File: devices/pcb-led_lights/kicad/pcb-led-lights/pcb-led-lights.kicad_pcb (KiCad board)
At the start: 2 copper layers, 61 x 30 mm, 29 parts, among them J1 Screw_Terminal_01x12, Q1 SUD40N06-25L, Q2 SUD40N06-25L, Q3 SUD40N06-25L, Q4 SUD40N06-25L, Q5 SUD40N06-25L, Q6 SUD40N06-25L, Q7 SUD40N06-25L, U1 AP63203WU, U2 ESP32-WROOM-32

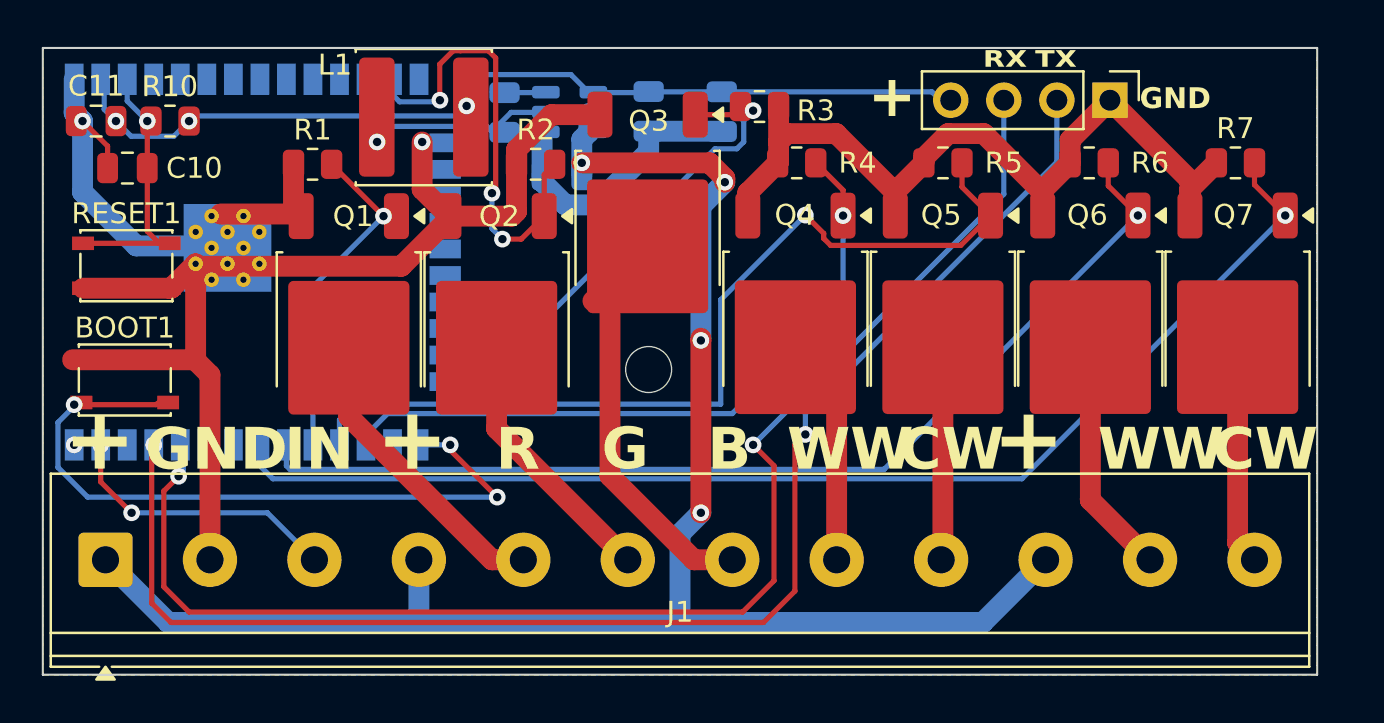
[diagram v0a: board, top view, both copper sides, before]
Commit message: use esp32-c6
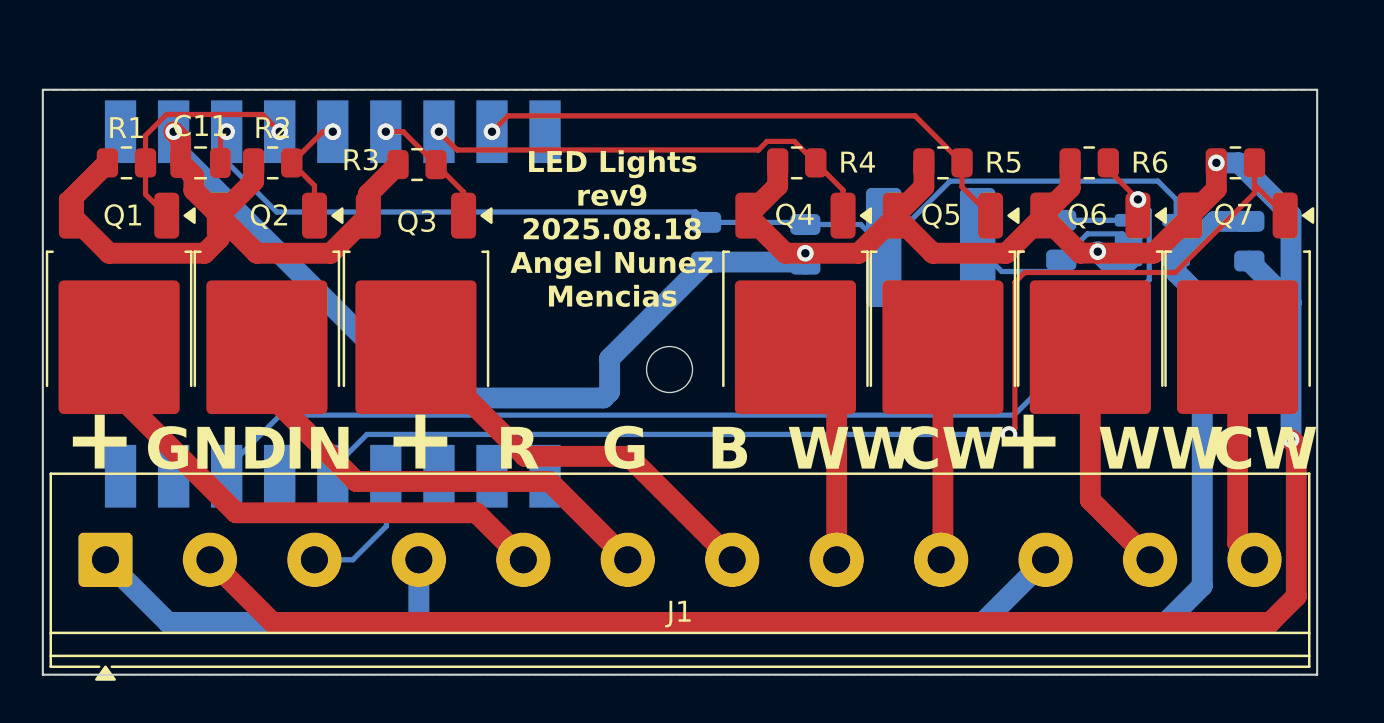
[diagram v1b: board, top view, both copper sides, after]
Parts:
- removed BOOT1, RESET1: SW_Push, Button_Switch_SMD:SW_SPST_PTS810
- removed C10: 10uF, Capacitor_SMD:C_0805_2012Metric
- removed R10: 12K, Resistor_SMD:R_0805_2012Metric
- removed U2: ESP32-WROOM-32, RF_Module:ESP32-WROOM-32
- removed program_port1: Conn_01x04_Male, Connector_PinHeader_2.54mm:PinHeader_1x04_P2.54mm_Vertical
- added U3: ESP32-C6 ZERO, Waveshare-ESP32:Waveshare-ESP32-C6-Zero, B.Cu at (47.6, 41.8)
- L1: moved to B.Cu
- moved C12 33.1 mm to (91.8, 39.2), turned to 90 degrees
- moved U1 28.6 mm to (87.1, 39.2)
- moved C1 27.3 mm to (82.8, 39.2)
- moved L1 25.1 mm to (76.5, 39.5), turned to 180 degrees
- moved R3 16.6 mm to (51.9, 35.6), turned to 0 degrees
- moved R2 12.6 mm to (45.0, 35.5)
- moved Q3 12.1 mm to (51.9, 43.1)
- moved Q1 11.0 mm to (37.7, 43.1)
- moved Q2 11.0 mm to (44.7, 43.1)
- moved C13 9.84 mm to (70.5, 39.4)
- moved R1 8.91 mm to (38.0, 35.5)
- moved C2 6.29 mm to (65.8, 39.3)
- moved C11 5.39 mm to (41.5, 35.5), turned to 180 degrees
- moved H1 1.00 mm to (64.0, 45.4), turned to 90 degrees
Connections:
- C11 pad 1: GND -> +3V3
- C11 pad 2: +3V3 -> GND
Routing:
- net TX: track 68.1 -> 0.00 mm, vias 2 -> 0
- net RX: track 65.9 -> 0.00 mm, vias 2 -> 0
- net GND: track 132.7 -> 191.1 mm, vias 3 -> 5
- net Net-(U2-IO0): track 34.1 -> 0.00 mm, vias 3 -> 0
- net P5: track 43.8 -> 26.8 mm
- net P2: track 22.1 -> 5.56 mm, vias 3 -> 1
- net P3: track 22.4 -> 6.05 mm
- net RESET: track 12.6 -> 0.00 mm, vias 1 -> 0
- net P4: track 33.2 -> 22.1 mm
- net O1: track 14.5 -> 24.9 mm
- net O2: track 12.8 -> 22.7 mm
- net +3V3: track 45.1 -> 52.9 mm, vias 3 -> 1
- net IN: track 13.5 -> 6.01 mm, vias 2 -> 0
- net P1: track 16.5 -> 11.4 mm
- net P6: track 50.0 -> 54.7 mm
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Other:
- board size 61 x 30 mm -> 61 x 28 mm
- board text removed: "RX"
- board text removed: "TX"

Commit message: add diode
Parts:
- added D1: US2MA, Diode_SMD:D_SMA, B.Cu at (89.5, 46.5)
- R1, R2, R3, R4, R5, R6, R7: value R -> 12K
- U3: value ESP32-C6 ZERO -> ~
- turned H1 to -90 degrees
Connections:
- C12 pad 2: VCC -> Net-(D1-K)
- U1 pad 2: VCC -> Net-(D1-K)
- U1 pad 3: VCC -> Net-(D1-K)
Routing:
- net VCC: track 83.7 -> 69.7 mm
- net Net-(D1-K): track 0.00 -> 7.53 mm
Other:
- board text added: "LED Lights rev10 2025.08.18 Angel Nunez Mencias"
- board text removed: "LED Lights rev9 2025.08.18 Angel Nunez Mencias"
